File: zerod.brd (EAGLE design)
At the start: 82.2 x 80 mm, 38 parts, among them IC1 NE5532N, IC2 LM3914N, Q1 2N3906

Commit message: new, smaller board
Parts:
- removed C2: 100uF, rcl:E22-6
- removed CY2: 10uF, rcl:E22-6
- added C3: 100uF, rcl:E22-6
- added C6: 10uF, rcl:E22-6
- moved D3 44.4 mm to (53.3, 34.3)
- moved CY3 43.3 mm to (55.9, 39.4)
- moved U$1 29.2 mm to (34.3, 29.2)
- moved C4 18.3 mm to (19.1, 39.4)
- moved IC1 18.1 mm to (27.9, 38.1), turned to 180 degrees
- moved C5 17.1 mm to (36.8, 36.8)
- moved R3 14.4 mm to (26.7, 44.5), turned to 180 degrees
- moved PAD4 14.2 mm to (14.0, 43.2)
- moved PAD3 14.2 mm to (3.81, 43.2)
- moved D2 12.0 mm to (11.4, 34.3)
- moved PAD1 11.7 mm to (3.81, 48.3)
- moved PAD2 11.7 mm to (14.0, 48.3)
- moved R2 11.4 mm to (58.4, 44.5), turned to 0 degrees
- moved CY1 8.98 mm to (44.5, 43.2)
- moved R15 8.98 mm to (16.5, 59.7)
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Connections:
- net +12V: now also C6.+; no longer CY2.+
- net GNDA: now also C6.-; no longer CY2.-
- net N$3: now also C3.-; no longer C2.-
- net N$5: now also C3.+; no longer C2.+
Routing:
- net GNDA: track 350.1 -> 288.2 mm
- net +12V: track 230.5 -> 268.1 mm
- net N$5: track 80.9 -> 49.3 mm
- net N$12: track 18.1 -> 36.6 mm
- net -12V: track 38.3 -> 46.4 mm
- net N$2: track 6.13 -> 14.1 mm
- net N$6: track 38.3 -> 31.1 mm
- net N$21: track 13.8 -> 8.45 mm
- net N$20: track 12.3 -> 6.88 mm
- net N$22: track 16.9 -> 11.5 mm
- net N$23: track 26.4 -> 21.6 mm
- net N$10: track 17.9 -> 14.1 mm
- net N$19: track 10.7 -> 7.40 mm
- net N$7: track 33.4 -> 30.1 mm
- net N$8: track 10.5 -> 7.40 mm
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- removed copper zone on layer 16, net _OUTLINES_
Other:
- board size 82.2 x 80 mm -> 82.2 x 72.4 mm

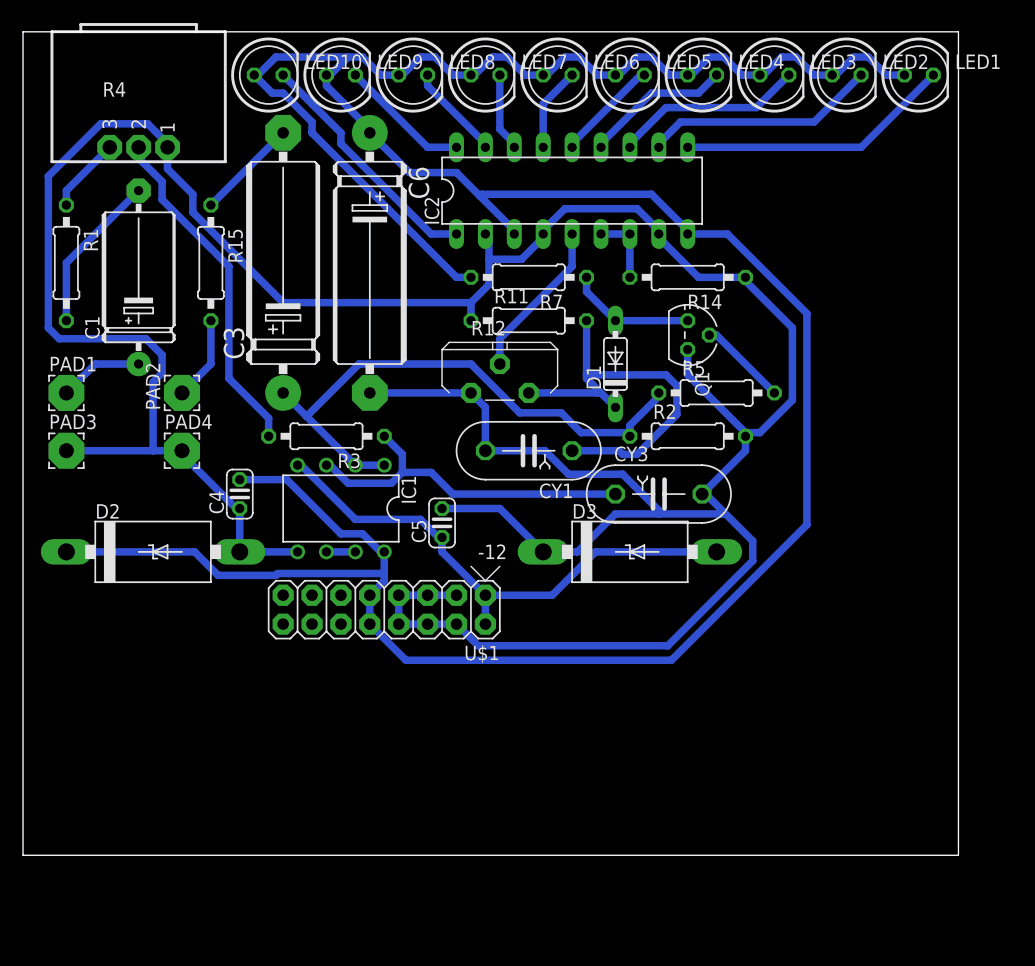
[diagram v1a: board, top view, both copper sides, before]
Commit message: thicker traces
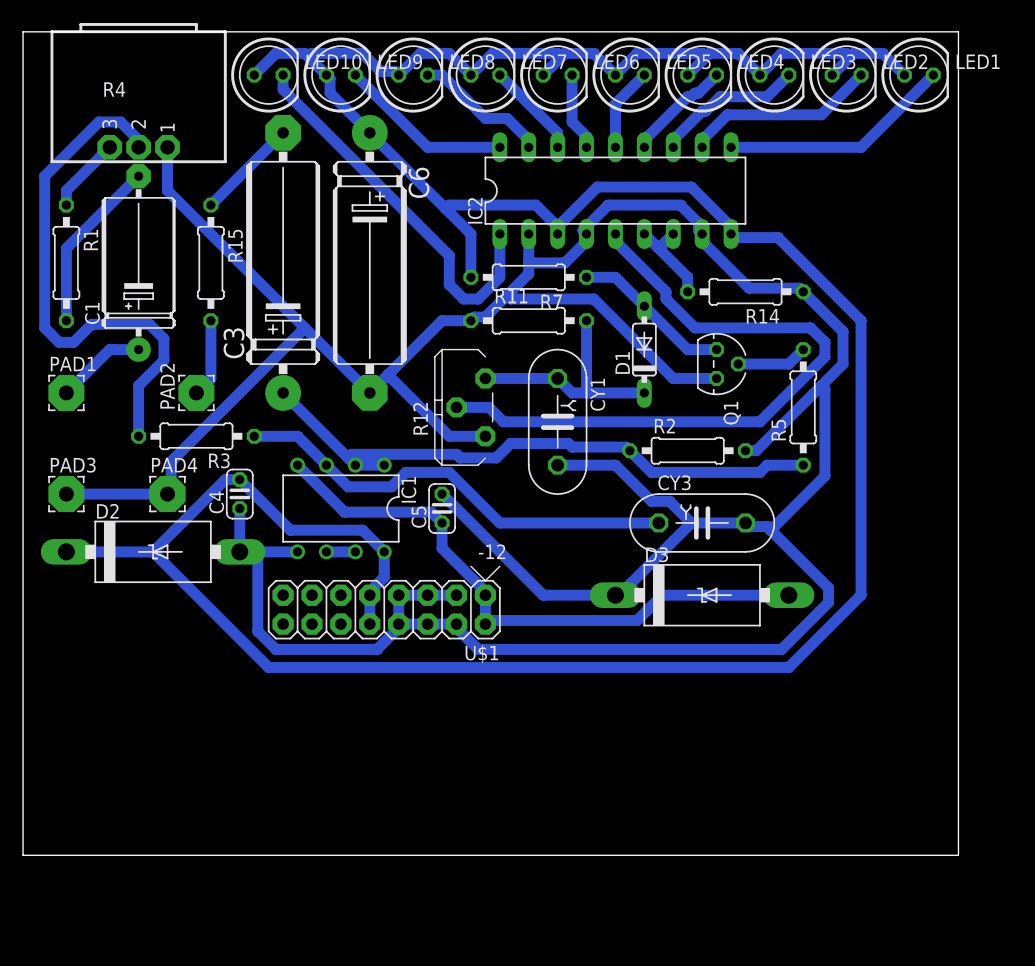
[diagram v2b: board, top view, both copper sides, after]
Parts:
- moved R3 11.4 mm to (15.2, 44.5)
- moved R5 7.73 mm to (68.6, 47.0), turned to 90 degrees
- moved D3 7.41 mm to (59.7, 30.5)
- moved R14 5.24 mm to (63.5, 57.1)
- moved CY3 4.58 mm to (59.7, 36.8)
- moved PAD4 4.02 mm to (12.7, 39.4)
- moved IC2 3.81 mm to (52.1, 66.0)
- moved PAD3 3.81 mm to (3.81, 39.4)
- moved Q1 3.59 mm to (61.0, 50.8)
- moved CY1 3.59 mm to (47.0, 45.7), turned to 270 degrees
- moved R12 3.59 mm to (39.4, 47.0), turned to 90 degrees
- moved D1 2.84 mm to (54.6, 52.1)
- moved C5 1.27 mm to (36.8, 38.1)
- moved R2 1.27 mm to (58.4, 43.2)
- moved PAD2 1.27 mm to (15.2, 48.3)
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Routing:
- net N$10: track 14.1 -> 59.7 mm
- net GNDA: track 288.2 -> 314.3 mm
- net N$7: track 30.1 -> 46.5 mm
- net N$12: track 36.6 -> 20.8 mm
- net N$23: track 21.6 -> 34.0 mm
- net N$6: track 31.1 -> 39.8 mm
- net +12V: track 268.1 -> 276.7 mm
- net -12V: track 46.4 -> 53.0 mm
- net N$5: track 49.3 -> 53.6 mm
- net N$22: track 11.5 -> 15.3 mm
- net N$11: track 24.2 -> 20.4 mm
- net N$17: track 13.0 -> 9.35 mm
- net N$13: track 20.6 -> 17.0 mm
- net N$16: track 16.8 -> 13.2 mm
- net N$21: track 8.45 -> 11.9 mm
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
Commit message: trimmer before peak detector
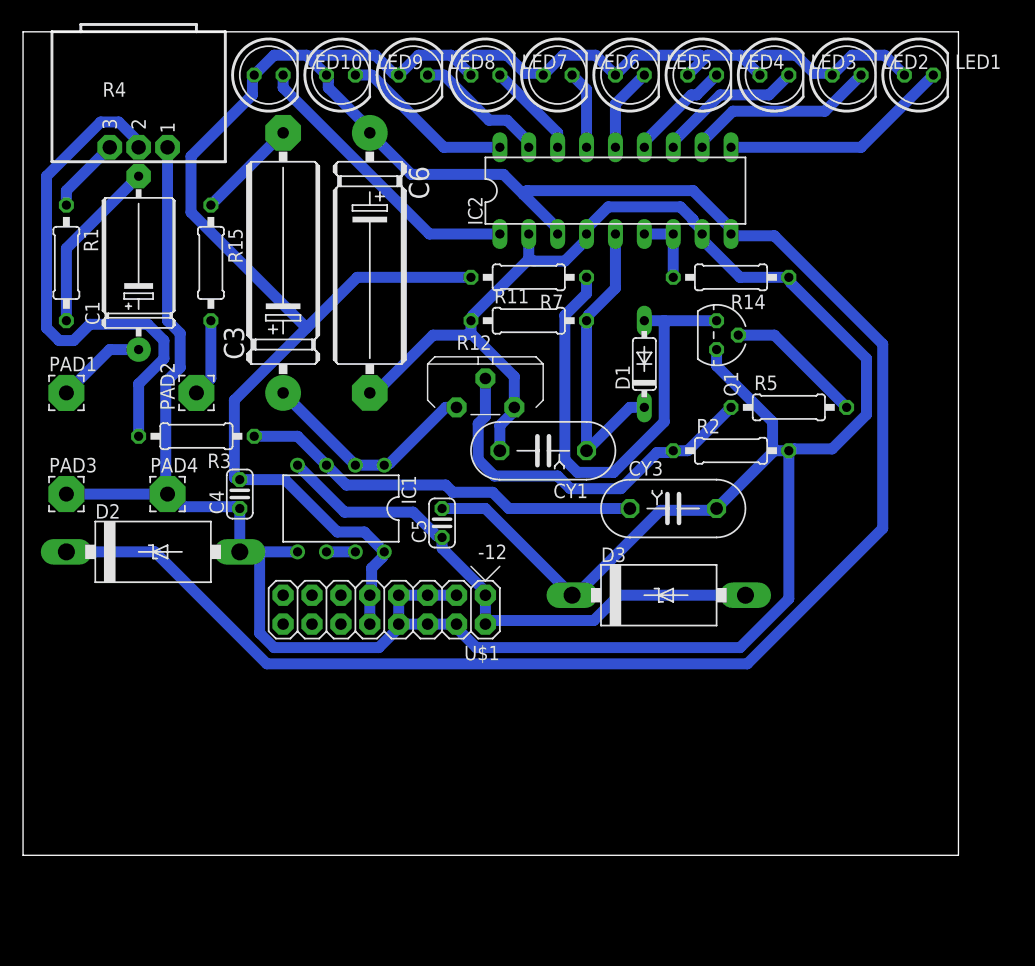
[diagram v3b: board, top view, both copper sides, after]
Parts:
- moved D3 3.81 mm to (55.9, 30.5)
- moved R2 3.81 mm to (62.2, 43.2)
- moved CY1 2.84 mm to (45.7, 43.2), turned to 180 degrees
- moved CY3 2.84 mm to (57.1, 38.1)
- moved Q1 2.54 mm to (61.0, 53.3)
- moved R14 1.80 mm to (62.2, 58.4)
- moved R12 1.80 mm to (40.6, 48.3), turned to 0 degrees
- moved C5 1.27 mm to (36.8, 36.8)
- moved D1 1.27 mm to (54.6, 50.8)
- moved R5 1.27 mm to (67.3, 47.0), turned to 0 degrees
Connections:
- net GNDA: now also R12.2; no longer R12.1
- net N$10: now also C3.+, IC1.1, IC1.2, R12.1; no longer IC2.5, R12.3
- net N$12: now also IC2.5; no longer R12.2
- net N$5: now also R12.3; no longer C3.+, IC1.1, IC1.2
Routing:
- net GNDA: track 314.3 -> 271.5 mm
- net +12V: track 276.7 -> 318.4 mm
- net N$10: track 59.7 -> 19.9 mm
- net N$15: track 14.1 -> 43.1 mm
- net N$5: track 53.6 -> 33.6 mm
- net N$23: track 34.0 -> 25.5 mm
- net N$9: track 6.24 -> 12.2 mm
- net N$12: track 20.8 -> 26.7 mm
- net -12V: track 53.0 -> 48.4 mm
- net N$6: track 39.8 -> 35.7 mm
- net N$14: track 8.45 -> 6.35 mm
- net N$7: track 46.5 -> 45.9 mm

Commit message: ditching the peak finder circuit
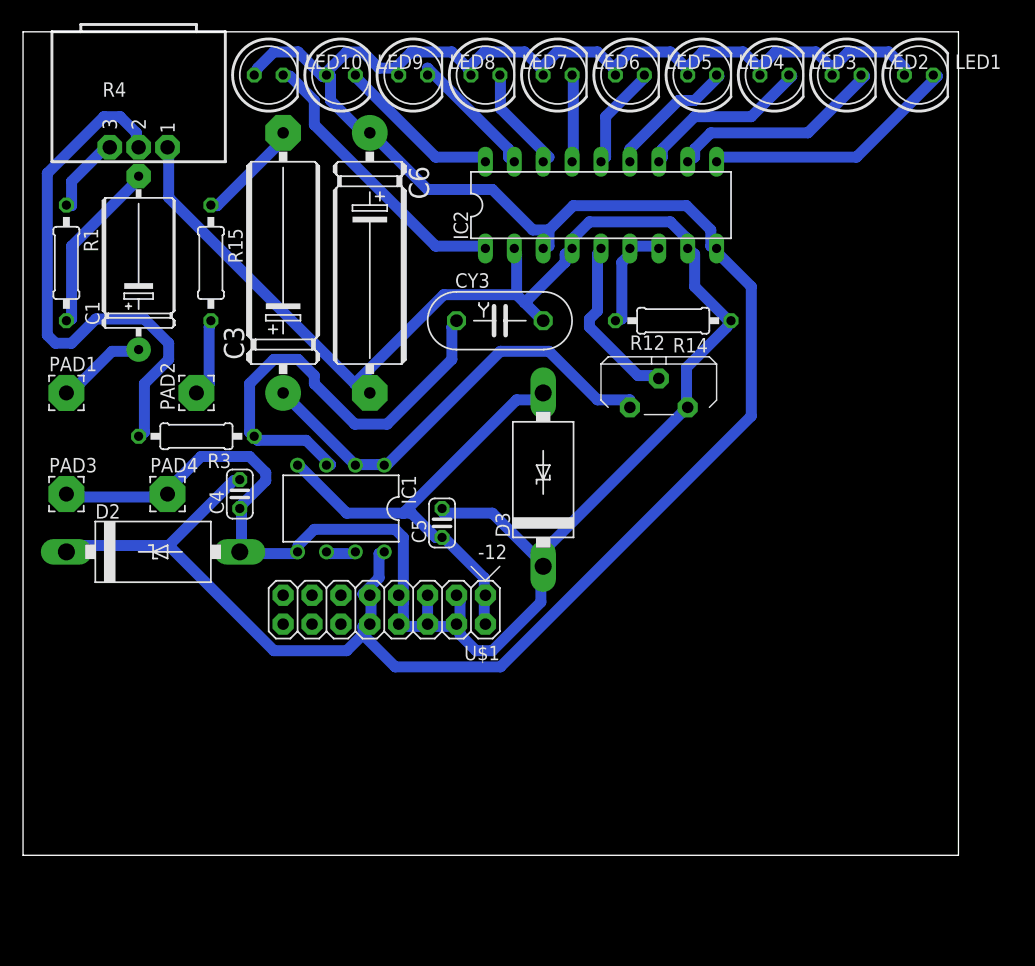
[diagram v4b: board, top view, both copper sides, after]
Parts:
- removed CY1: .1uF, rcl:YC7B5
- removed D1: 1N4148DO35-7, diode:DO35-7
- removed Q1: 2N3906, transistor-pnp:TO92
- removed R11: 1M, rcl:0207/10
- removed R2: 100k, rcl:0207/10
- removed R5: 1k, rcl:0207/10
- removed R7: 10k, rcl:0207/10
- moved CY3 22.5 mm to (41.9, 54.6)
- moved R12 15.2 mm to (55.9, 48.3)
- moved D3 14.4 mm to (45.7, 40.6), turned to 90 degrees
- moved R14 6.35 mm to (57.1, 54.6)
- moved IC2 1.80 mm to (50.8, 64.8)
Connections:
- removed net N$15: D1.A, Q1.3, R7.1
- removed net N$5: R12.3, R2.1, R5.1
- removed net N$9: Q1.2, R5.2
- net +12V: no longer R7.2
- net GNDA: no longer CY1.2, Q1.1, R11.1, R2.2
- net N$12: now also R12.3; no longer CY1.1, D1.C, R11.2
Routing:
- net +12V: track 318.4 -> 229.5 mm
- net GNDA: track 271.5 -> 199.2 mm
- net N$15: track 43.1 -> 0.00 mm
- net N$5: track 33.6 -> 0.00 mm
- net N$10: track 19.9 -> 39.7 mm
- net N$9: track 12.2 -> 0.00 mm
- net N$12: track 26.7 -> 15.2 mm
- net -12V: track 48.4 -> 41.5 mm
- net N$6: track 35.7 -> 40.2 mm
- net N$14: track 6.35 -> 9.86 mm
- net N$11: track 20.4 -> 23.0 mm
- net N$17: track 9.26 -> 11.8 mm
- net N$13: track 16.9 -> 19.4 mm
- net N$16: track 13.1 -> 15.5 mm
- net N$7: track 45.9 -> 48.1 mm
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
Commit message: no peak finder and balanced
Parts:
- removed R15: 51, rcl:0207/10
- removed U$1: POWER, eurorack:POWER_16
- added C2: (no value), capacitor-wima:C2.5-6
- added R2, R7: 10k, rcl:0207/10
- added R5, R6: 150, rcl:0207/10
- added U$2: POWER_SIMPLE10, eurorack:POWER_10
- C6: device rcl:E22-6 -> rcl:E1,8-4
- PAD2: value output -> output TIP
- PAD4: value output -> output RING
- moved C3 43.2 mm to (62.2, 41.9), turned to 0 degrees
- moved D3 25.3 mm to (69.8, 33.0), turned to 180 degrees
- moved C4 24.4 mm to (43.2, 35.6), turned to 180 degrees
- moved D2 18.5 mm to (29.2, 29.2), turned to 180 degrees
- moved R3 17.3 mm to (25.4, 58.4)
- moved C5 17.0 mm to (29.2, 52.1), turned to 270 degrees
- moved IC1 16.3 mm to (40.6, 48.3)
- moved R14 14.5 mm to (71.1, 50.8)
- moved IC2 13.3 mm to (63.5, 61.0)
- moved C6 9.92 mm to (22.9, 66.0), turned to 180 degrees
- moved PAD4 7.62 mm to (5.08, 39.4)
- moved PAD3 6.35 mm to (10.2, 39.4)
- moved PAD2 5.68 mm to (10.2, 45.7), turned to 0 degrees
- moved CY3 5.68 mm to (39.4, 59.7)
- moved R1 4.02 mm to (5.08, 55.9)
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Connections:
- removed net N$24: IC1.6, IC1.7
- new net N$15: PAD2.1, R5.2, R7.2
- new net N$5: PAD4.1, R6.2
- new net N$9: C2.2, IC1.7, R5.1
- net +12V: now also U$2.10, U$2.9; no longer U$1.10, U$1.9
- net -12V: now also U$2.1, U$2.2; no longer U$1.1, U$1.2
- net GNDA: now also R6.1, U$2.3, U$2.4, U$2.5, U$2.6, U$2.7, U$2.8; no longer PAD4.1, U$1.3, U$1.4, U$1.5, U$1.6, U$1.7, U$1.8
- net N$3: now also R2.1; no longer R15.1
- net N$8: now also C2.1, IC1.6, R2.2, R7.1; no longer PAD2.1, R15.2
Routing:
- net GNDA: track 199.2 -> 288.4 mm
- net N$3: track 10.2 -> 62.3 mm
- net N$9: track 0.00 -> 37.1 mm
- net N$6: track 40.2 -> 14.5 mm
- net N$8: track 6.98 -> 26.2 mm
- net N$15: track 0.00 -> 18.4 mm
- net N$22: track 14.9 -> 28.9 mm
- net N$21: track 12.0 -> 25.4 mm
- net N$23: track 25.4 -> 38.4 mm
- net N$20: track 9.64 -> 21.6 mm
- net N$10: track 39.7 -> 28.8 mm
- net N$19: track 7.67 -> 17.8 mm
- net N$5: track 0.00 -> 8.89 mm
- net -12V: track 41.5 -> 49.6 mm
- net +12V: track 229.5 -> 236.8 mm
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
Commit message: value set for output filter cap
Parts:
- C2: value (none) -> 100pF
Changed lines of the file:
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@@
 <element name="R6" library="rcl" package="0207/10" value="150" x="10.16" y="30.48" rot="R180"/>
 <element name="R7" library="rcl" package="0207/10" value="10k" x="22.86" y="40.64" rot="R270"/>
-<element name="C2" library="capacitor-wima" package="C2.5-6" value="" x="21.59" y="53.34" rot="R180"/>
+<element name="C2" library="capacitor-wima" package="C2.5-6" value="100pF" x="21.59" y="53.34" rot="R180"/>
 </elements>
 <signals>

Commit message: regen gcode with new schema
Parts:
- removed C3: 100uF, rcl:E22-6
- R1, R4: value 5k -> 50k
- moved R2 10.2 mm to (33.0, 49.5), turned to 270 degrees
- moved D3 9.67 mm to (66.0, 41.9)
- moved C4 4.02 mm to (41.9, 39.4)
- moved U$2 3.59 mm to (53.3, 31.8)
- moved C5 2.54 mm to (29.2, 49.5)
- moved D2 1.80 mm to (30.5, 30.5)
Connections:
- removed net N$3: C3.-, R2.1
- net N$10: now also R2.1; no longer C3.+
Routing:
- net +12V: track 236.8 -> 324.8 mm
- net N$3: track 62.3 -> 0.00 mm
- net GNDA: track 288.4 -> 235.3 mm
- net -12V: track 49.6 -> 58.4 mm
- net N$11: track 18.6 -> 14.1 mm
- net N$10: track 28.8 -> 30.4 mm
- net N$9: track 37.1 -> 36.2 mm
